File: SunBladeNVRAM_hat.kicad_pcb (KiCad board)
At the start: 2 copper layers, 36.5 x 18.5 mm, 5 parts, among them J105 Conn_01x01_Pin, J106 Conn_01x01_Pin, J107 Conn_01x01_Pin, J108 Conn_01x01_Pin

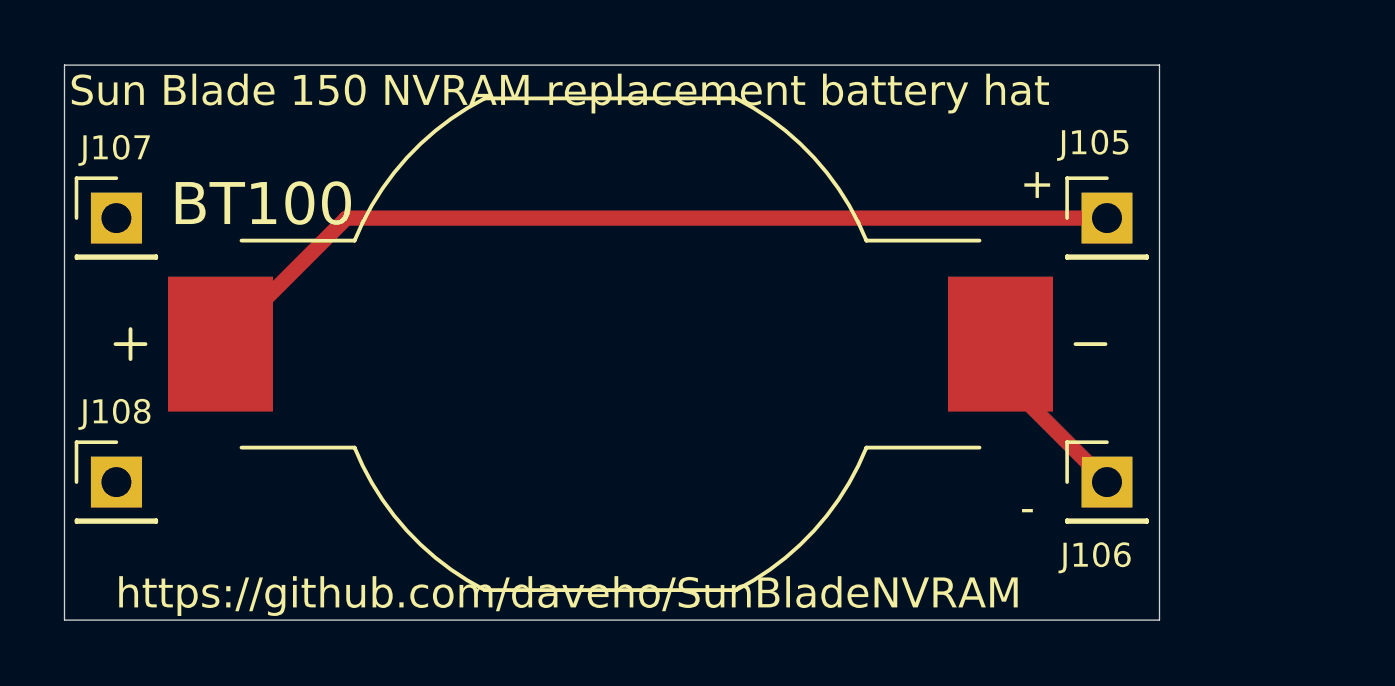
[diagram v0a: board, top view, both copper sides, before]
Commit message: use correct M48T59Y-MH footprint
Changed pin headers to be surface mount, meaning the
pads can be on the bottom and so not interfere with the
M49T59Y.

Bottom PCB needs to be a bit larger, and the top
(battery hat) PCB also needed a minor redesign.

Still need to route the connections.
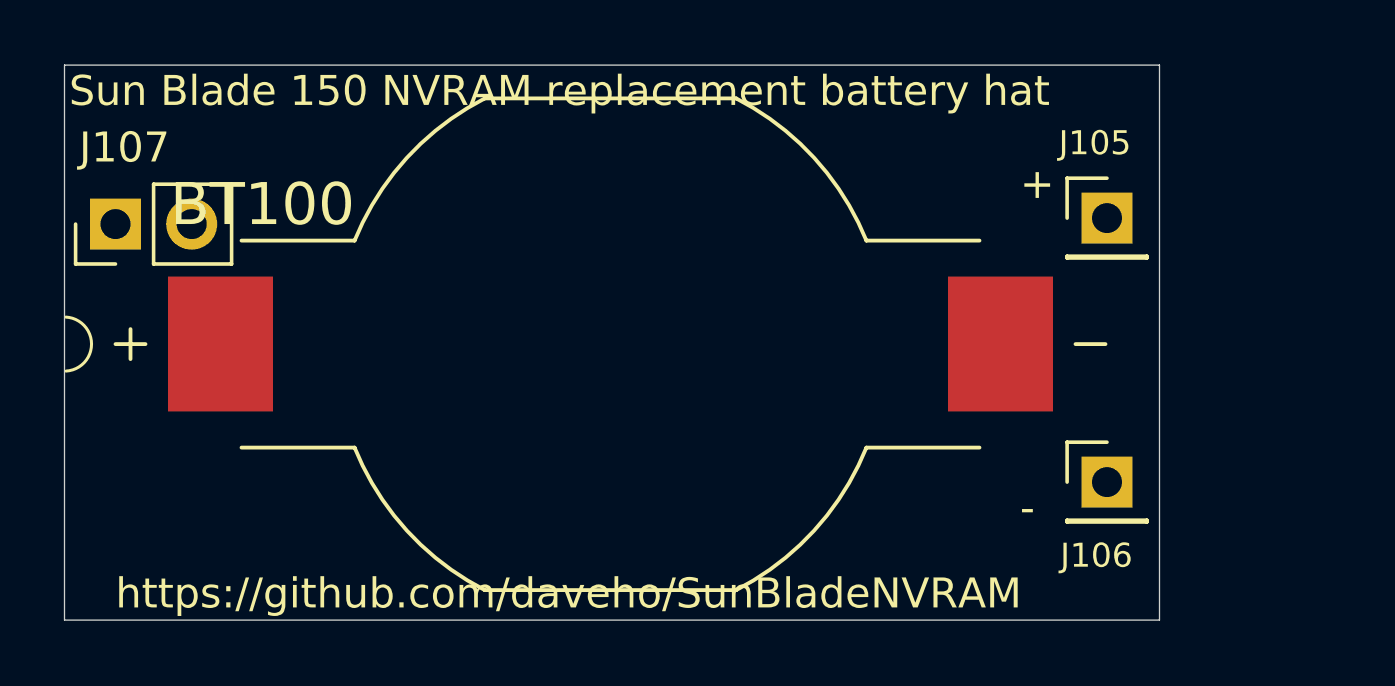
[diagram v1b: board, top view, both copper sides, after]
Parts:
- removed J108: Conn_01x01_Pin, Connector_PinHeader_2.54mm:PinHeader_1x01_P2.54mm_Vertical
- J107: value Conn_01x01_Pin -> Conn_01x02_Pin; footprint Connector_PinHeader_2.54mm:PinHeader_1x01_P2.54mm_Vertical -> Connector_PinHeader_2.54mm:PinHeader_1x02_P2.54mm_Vertical
- moved J107 0.20 mm to (85.0, 75.1), turned to 90 degrees
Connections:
- J107 pad 1: unconnected-(J107-Pin_1-Pad1) -> (no net)
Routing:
- net Net-(J105-Pin_1): track 31.3 -> 0.00 mm
- net Net-(J106-Pin_1): track 6.07 -> 1.05 mm
